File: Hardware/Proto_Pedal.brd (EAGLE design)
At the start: 85.1 x 110.5 mm, 124 parts, among them J1 POWER_JACKSMD_FIXED, Q1 2.5A/30V, SW1 SWITCH-3PDT

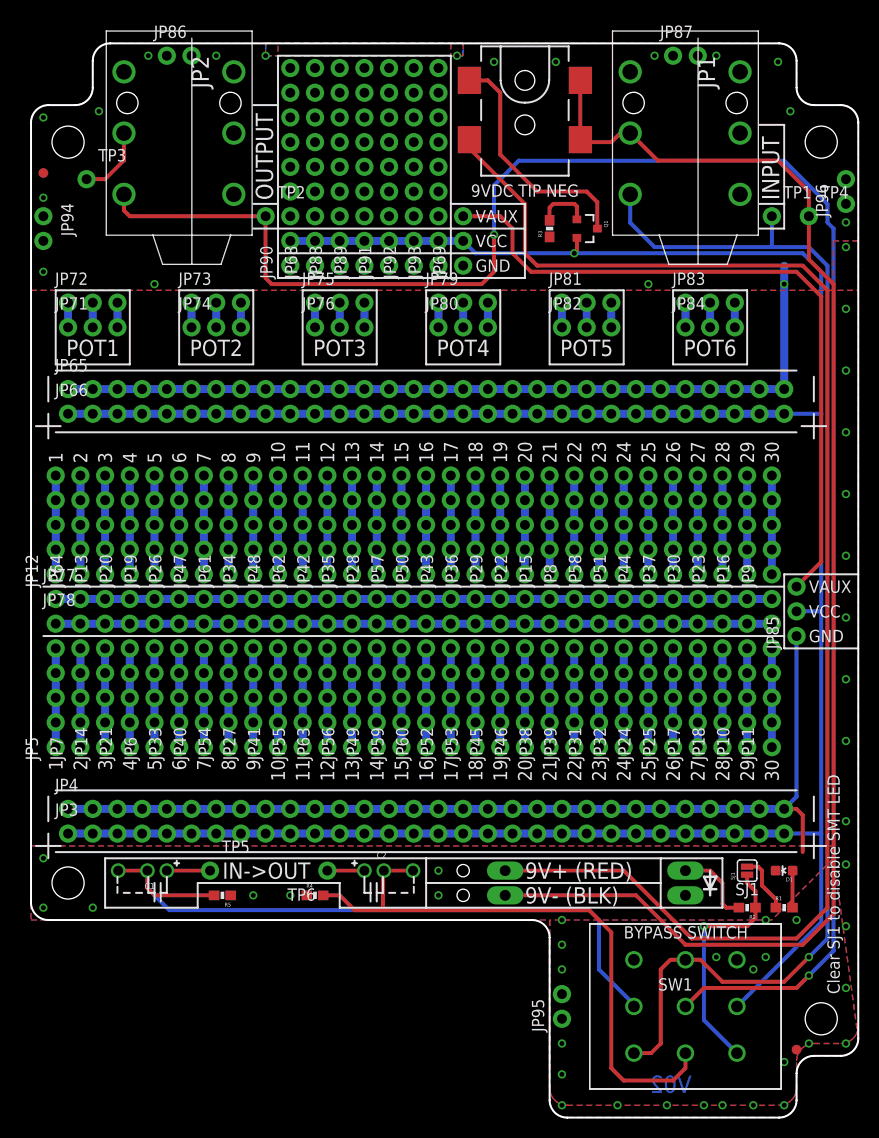
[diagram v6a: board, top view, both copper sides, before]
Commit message: Updates after group review.
PTH power connector.
PTH LED bias resistor.
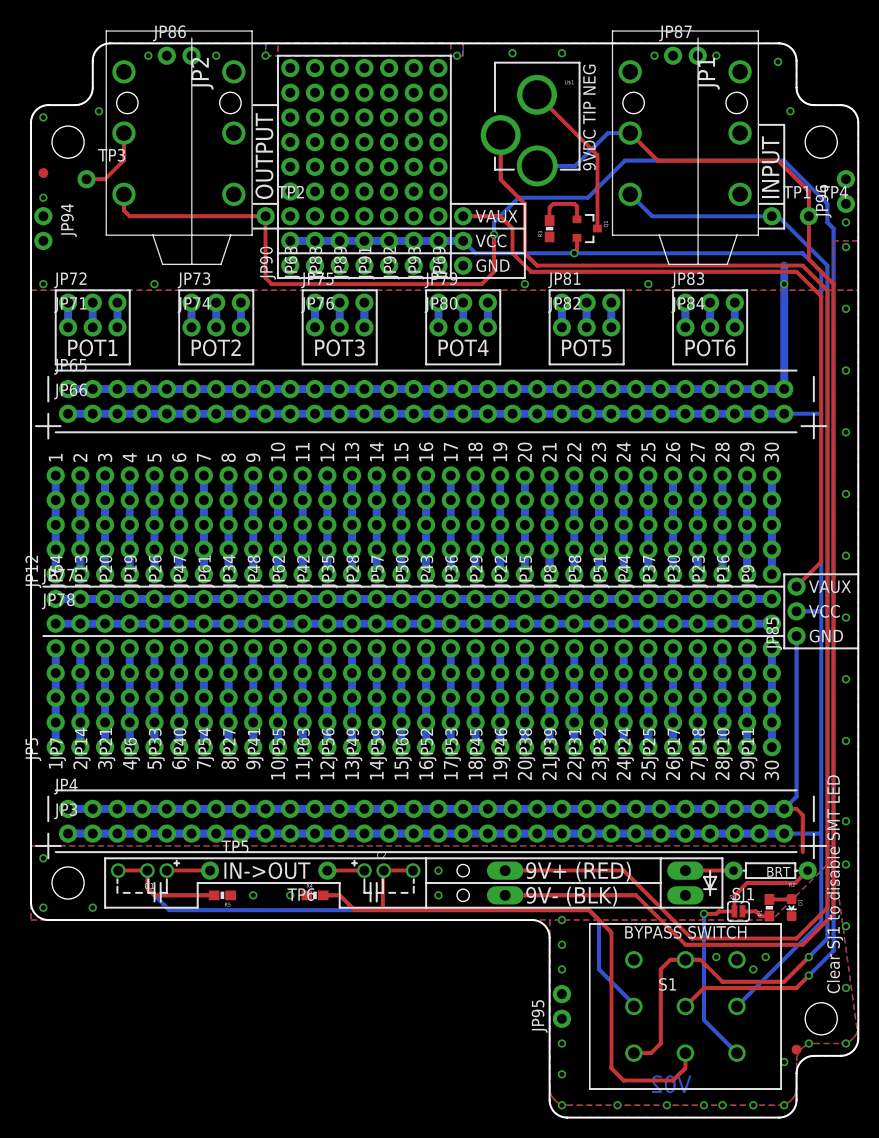
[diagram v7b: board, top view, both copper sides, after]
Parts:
- removed J1: POWER_JACKSMD_FIXED, Testing:POWER_JACK_SMD
- added U$1: POWER_JACK_TIP_NEGATIVE, Testing:POWER-BARRELJACK-PTH-LOCK-FIXED
- R2: value 1K -> BRT; device SparkFun-Resistors:0603-RES -> SparkFun-Resistors:AXIAL-0.3
- moved R2 4.51 mm to (76.1, 25.4)
- moved SJ1 4.28 mm to (72.8, 21.2), turned to 0 degrees
- moved D1 3.89 mm to (78.2, 21.6), turned to 180 degrees
- moved R1 1.52 mm to (75.9, 21.6), turned to 90 degrees
- renumbered SW1 to S1
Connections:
- net LEDA: now also R2.P$2; no longer R2.2
- net N$35: now also R2.P$1; no longer R2.1
- net N$45: now also U$1.SLEEVE-NORMAL; no longer J1.P$4
- net N$55: now also U$1.TIP; no longer J1.VIN0, J1.VIN1
- net VBATT: now also U$1.SLEEVE; no longer J1.GND
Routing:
- net VBATT: track 24.8 -> 16.3 mm
- net N$70: track 128.5 -> 123.7 mm
- net N$35: track 24.9 -> 29.2 mm
- net LEDA: track 8.34 -> 4.95 mm
- net N$65: track 6.10 -> 2.96 mm
- net N$71: track 187.9 -> 185.6 mm
- net N$25: track 3.82 -> 2.30 mm
- net N$45: track 147.6 -> 146.7 mm
- net N$55: track 145.1 -> 144.4 mm
- net GND: vias 58 -> 57

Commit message: Relaxed design to use standard DRU
Fixed funny pour shapes
Relocated a couple traces
Renumbered parts
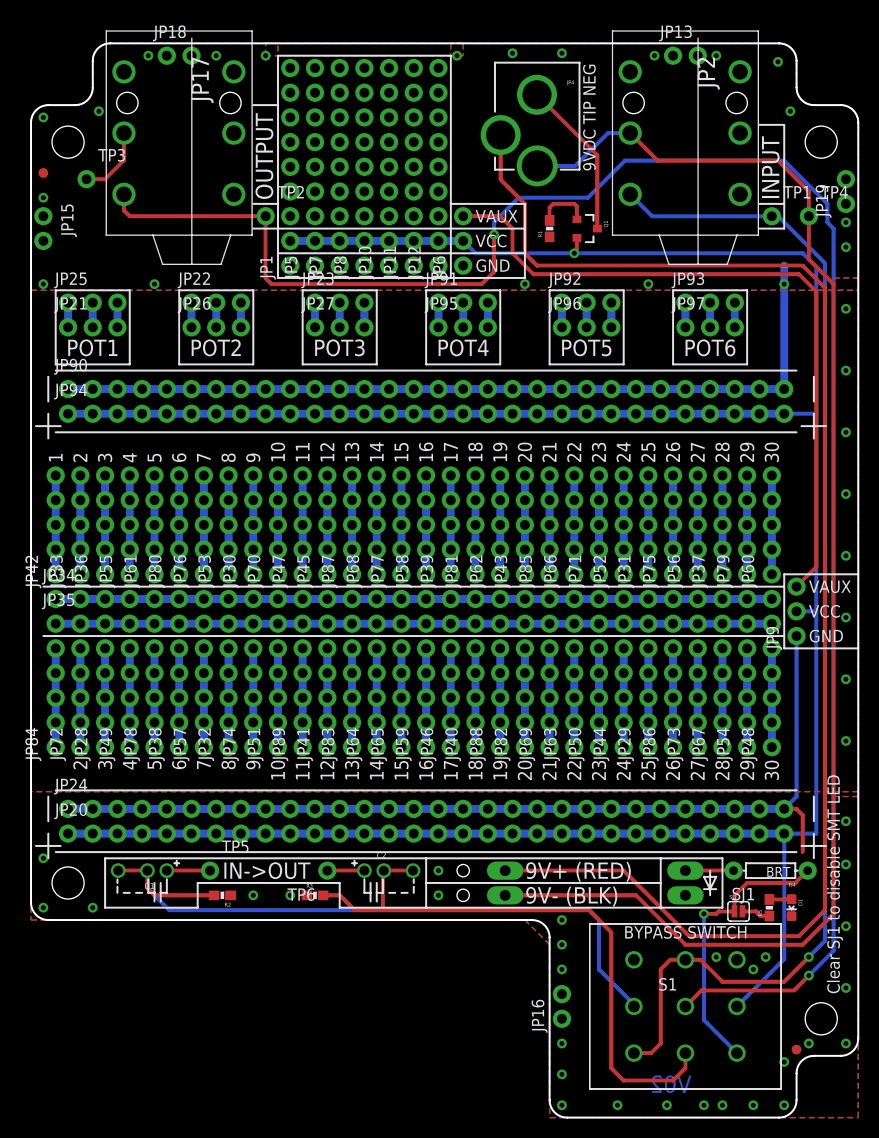
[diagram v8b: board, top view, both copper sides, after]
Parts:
- removed D2: PTH-LED, SparkFun-Connectors:1X02_LONGPADS
- removed U$1: POWER_JACK_TIP_NEGATIVE, Testing:POWER-BARRELJACK-PTH-LOCK-FIXED
- added JP67: 1x5, SparkFun-Connectors:1X05_NO_SILK
- added JP97: 1x3, SparkFun-Connectors:1X03_NO_SILK
- JP1: value INPUT JACK -> 1x9; device SparkFun-Connectors:AUDIO-JACK-.25-INCH-HORIZ-PTH -> SparkFun-Connectors:1X09_NO_SILK
- JP10, JP11, JP12, JP5, JP7, JP8: value 1x5 -> 1x9; device SparkFun-Connectors:1X05_NO_SILK -> SparkFun-Connectors:1X09_NO_SILK
- JP13, JP15, JP16, JP18, JP19: value 1x5 -> 1x2; device SparkFun-Connectors:1X05_NO_SILK -> SparkFun-Connectors:1X02_NO_SILK
- JP14: value 1x5 -> PTH-LED; device SparkFun-Connectors:1X05_NO_SILK -> SparkFun-Connectors:1X02_LONGPADS
- JP17: value 1x5 -> OUTPUT JACK; device SparkFun-Connectors:1X05_NO_SILK -> SparkFun-Connectors:AUDIO-JACK-.25-INCH-HORIZ-PTH
- JP2: value OUTPUT JACK -> INPUT JACK
- JP20, JP24, JP34, JP35: value 1x5 -> 1x30; device SparkFun-Connectors:1X05_NO_SILK -> SparkFun-Connectors:1X30_NO_SILK
- JP21, JP22, JP23, JP25, JP26, JP27, JP6, JP9: value 1x5 -> 1x3; device SparkFun-Connectors:1X05_NO_SILK -> SparkFun-Connectors:1X03_NO_SILK
- JP3: value 1x30 -> 9VBattery; device SparkFun-Connectors:1X30_NO_SILK -> SparkFun-Connectors:1X02_LONGPADS
- JP4: value 1x30 -> POWER_JACK_TIP_NEGATIVE; device SparkFun-Connectors:1X30_NO_SILK -> Testing:POWER-BARRELJACK-PTH-LOCK-FIXED
- JP55: value v -> 1x5
- JP65, JP66, JP77, JP78: value 1x30 -> 1x5; device SparkFun-Connectors:1X30_NO_SILK -> SparkFun-Connectors:1X05_NO_SILK
- JP68, JP88: value 1x9 -> 1x5; device SparkFun-Connectors:1X09_NO_SILK -> SparkFun-Connectors:1X05_NO_SILK
- JP69, JP71, JP72, JP73, JP74, JP75, JP76, JP79, JP80, JP81, JP82, JP83, JP84, JP85: value 1x3 -> 1x5; device SparkFun-Connectors:1X03_NO_SILK -> SparkFun-Connectors:1X05_NO_SILK
- JP70: value 9VBattery -> 1x5; device SparkFun-Connectors:1X02_LONGPADS -> SparkFun-Connectors:1X05_NO_SILK
- JP86, JP87: value 1x2 -> 1x5; device SparkFun-Connectors:1X02_NO_SILK -> SparkFun-Connectors:1X05_NO_SILK
- JP89: value 1x9 -> v; device SparkFun-Connectors:1X09_NO_SILK -> SparkFun-Connectors:1X05_NO_SILK
- JP90: value 1x9 -> 1x30; device SparkFun-Connectors:1X09_NO_SILK -> SparkFun-Connectors:1X30_NO_SILK
- JP91, JP92, JP93: value 1x9 -> 1x3; device SparkFun-Connectors:1X09_NO_SILK -> SparkFun-Connectors:1X03_NO_SILK
- JP94: value 1x2 -> 1x30; device SparkFun-Connectors:1X02_NO_SILK -> SparkFun-Connectors:1X30_NO_SILK
- JP95, JP96: value 1x2 -> 1x3; device SparkFun-Connectors:1X02_NO_SILK -> SparkFun-Connectors:1X03_NO_SILK
- R1: value 1K -> 1M
- R2: value BRT -> 1M; device SparkFun-Resistors:AXIAL-0.3 -> SparkFun-Resistors:0603-RES
- R4: value 1M -> BRT; device SparkFun-Resistors:0603-RES -> SparkFun-Resistors:AXIAL-0.3
- R5: value 1M -> 1K
- moved FID1 118.9 mm to (78.7, 6.99)
- moved FID2 118.9 mm to (1.27, 97.2)
- moved STANDOFF2 108.7 mm to (3.81, 24.1)
- moved JP4 93.4 mm to (52.1, 111.8), turned to 180 degrees
- moved JP18 91.2 mm to (14.0, 109.2), turned to 0 degrees
- moved JP17 90.2 mm to (16.5, 111.8), turned to 270 degrees
- moved JP86 88.1 mm to (66.0, 38.1), turned to 90 degrees
- moved JP19 80.7 mm to (83.8, 94.0)
- moved JP13 79.1 mm to (66.0, 109.2), turned to 0 degrees
- moved JP84 77.8 mm to (2.54, 38.1), turned to 90 degrees
- moved STANDOFF3 77.5 mm to (81.3, 100.3)
- moved JP25 77.2 mm to (3.81, 83.8), turned to 0 degrees
- moved STANDOFF4 76.2 mm to (3.81, 100.3)
- moved R1 73.4 mm to (53.3, 91.4)
- moved R3 72.7 mm to (29.2, 22.9), turned to 0 degrees
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- renumbered LOGO3 to LOGO2
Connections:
- removed net N$10 (its old number): JP9.1, JP9.2, JP9.3, JP9.4, JP9.5
- removed net N$11 (its old number): JP11.1, JP11.2, JP11.3, JP11.4, JP11.5
- removed net N$12 (its old number): JP12.1, JP12.2, JP12.3, JP12.4, JP12.5
- removed net N$13 (its old number): JP13.1, JP13.2, JP13.3, JP13.4, JP13.5
- removed net N$14 (its old number): JP14.1, JP14.2, JP14.3, JP14.4, JP14.5
- removed net N$19 (its old number): JP19.1, JP19.2, JP19.3, JP19.4, JP19.5
- removed net N$20 (its old number): JP20.1, JP20.2, JP20.3, JP20.4, JP20.5
- removed net N$21 (its old number): JP21.1, JP21.2, JP21.3, JP21.4, JP21.5
- removed net N$22 (its old number): JP22.1, JP22.2, JP22.3, JP22.4, JP22.5
- removed net N$23 (its old number): JP23.1, JP23.2, JP23.3, JP23.4, JP23.5
- removed net N$24 (its old number): JP24.1, JP24.2, JP24.3, JP24.4, JP24.5
- removed net N$34 (its old number): JP34.1, JP34.2, JP34.3, JP34.4, JP34.5
- removed net N$5 (its old number): JP10.1, JP10.2, JP10.3, JP10.4, JP10.5
- new net N$15: JP89.1, JP89.2, JP89.3, JP89.4, JP89.5
- new net N$28: JP68.1, JP68.2, JP68.3, JP68.4, JP68.5
- new net N$36: JP81.1, JP81.2, JP81.3, JP81.4, JP81.5
- new net N$37: JP75.1, JP75.2, JP75.3, JP75.4, JP75.5
- new net N$38: JP69.1, JP69.2, JP69.3, JP69.4, JP69.5
- new net N$46: JP82.1, JP82.2, JP82.3, JP82.4, JP82.5
- new net N$47: JP76.1, JP76.2, JP76.3, JP76.4, JP76.5
- new net N$48: JP70.1, JP70.2, JP70.3, JP70.4, JP70.5
- new net N$56: JP83.1, JP83.2, JP83.3, JP83.4, JP83.5
- new net N$57: JP77.1, JP77.2, JP77.3, JP77.4, JP77.5
- new net N$58: JP71.1, JP71.2, JP71.3, JP71.4, JP71.5
- new net N$59: JP65.1, JP65.2, JP65.3, JP65.4, JP65.5
- new net N$6: JP88.1, JP88.2, JP88.3, JP88.4, JP88.5
- net FX_IN: now also R2.2; no longer R5.2
- net FX_OUT: now also R3.2; no longer R4.2
- net GND: now also JP1.1, JP10.1, JP11.1, JP12.1, JP13.1, JP13.2, JP14.2, JP15.1, JP15.2, JP16.1, JP16.2, JP17.SLEEVE, JP18.1, JP18.2, JP19.1, JP19.2, JP2.TIP-NORM, JP24.1, JP24.10, JP24.11, JP24.12, JP24.13, JP24.14, JP24.15, JP24.16, JP24.17, JP24.18, JP24.19, JP24.2, JP24.20, JP24.21, JP24.22, JP24.23, JP24.24, JP24.25, JP24.26, JP24.27, JP24.28, JP24.29, JP24.3, JP24.30, JP24.4, JP24.5, JP24.6, JP24.7, JP24.8, JP24.9, JP5.1, JP6.1, JP7.1, JP8.1, JP9.1, JP90.10, JP90.11, JP90.12, JP90.13, JP90.14, JP90.15, JP90.16, JP90.17, JP90.18, JP90.19, JP90.2, JP90.20, JP90.21, JP90.22, JP90.23, JP90.24, JP90.25, JP90.26, JP90.27, JP90.28, JP90.29, JP90.3, JP90.30, JP90.4, JP90.5, JP90.6, JP90.7, JP90.8, JP90.9, R1.1, R2.1; no longer D2.2, JP1.SLEEVE, JP1.TIP-NORM, JP4.1, JP4.10, JP4.11, JP4.12, JP4.13, JP4.14, JP4.15, JP4.16, JP4.17, JP4.18, JP4.19, JP4.2, JP4.20, JP4.21, JP4.22, JP4.23, JP4.24, JP4.25, JP4.26, JP4.27, JP4.28, JP4.29, JP4.3, JP4.30, JP4.4, JP4.5, JP4.6, JP4.7, JP4.8, JP4.9, JP65.1, JP65.10, JP65.11, JP65.12, JP65.13, JP65.14, JP65.15, JP65.16, JP65.17, JP65.18, JP65.19, JP65.2, JP65.20, JP65.21, JP65.22, JP65.23, JP65.24, JP65.25, JP65.26, JP65.27, JP65.28, JP65.29, JP65.3, JP65.30, JP65.4, JP65.5, JP65.6, JP65.7, JP65.8, JP65.9, JP68.1, JP69.1, JP85.1, JP86.1, JP86.2, JP87.1, JP87.2, JP88.1, JP89.1, JP91.1, JP92.1, JP93.1, JP94.1, JP94.2, JP95.1, JP95.2, JP96.1, JP96.2, R4.1, R5.1
- net LEDA: now also JP14.1, R4.P$2; no longer D2.1, R2.P$2
- net N$1: now also JP84.1, JP84.2, JP84.3, JP84.4, JP84.5; no longer JP5.1, JP5.2, JP5.3, JP5.4, JP5.5
- net N$100: now also JP92.3, JP96.3; no longer JP81.3, JP82.3
- net N$101: now also JP93.1, JP97.1; no longer JP83.1, JP84.1
- net N$102: now also JP93.2, JP97.2; no longer JP83.2, JP84.2
- net N$103: now also JP93.3, JP97.3; no longer JP83.3, JP84.3
- net N$16: now also JP79.1, JP79.2, JP79.3, JP79.4, JP79.5; no longer JP16.1, JP16.2, JP16.3, JP16.4, JP16.5
- net N$17: now also JP73.1, JP73.2, JP73.3, JP73.4, JP73.5; no longer JP17.1, JP17.2, JP17.3, JP17.4, JP17.5
- net N$18: now also JP67.1, JP67.2, JP67.3, JP67.4, JP67.5; no longer JP18.1, JP18.2, JP18.3, JP18.4, JP18.5
- net N$2: now also JP85.1, JP85.2, JP85.3, JP85.4, JP85.5; no longer JP15.1, JP15.2, JP15.3, JP15.4, JP15.5
- net N$25: now also R5.2; no longer R1.2
- net N$26: now also JP80.1, JP80.2, JP80.3, JP80.4, JP80.5; no longer JP26.1, JP26.2, JP26.3, JP26.4, JP26.5
- net N$27: now also JP74.1, JP74.2, JP74.3, JP74.4, JP74.5; no longer JP27.1, JP27.2, JP27.3, JP27.4, JP27.5
- net N$3: now also JP86.1, JP86.2, JP86.3, JP86.4, JP86.5; no longer JP25.1, JP25.2, JP25.3, JP25.4, JP25.5
- net N$35: now also R4.P$1; no longer R2.P$1
- net N$4: now also JP87.1, JP87.2, JP87.3, JP87.4, JP87.5; no longer JP35.1, JP35.2, JP35.3, JP35.4, JP35.5
- net N$45: now also JP3.1, JP4.SLEEVE-NORMAL; no longer JP70.1, U$1.SLEEVE-NORMAL
- net N$55: now also JP2.RING, JP3.2, JP4.TIP; no longer JP1.RING, JP70.2, U$1.TIP
- net N$65: now also R5.1; no longer R1.1
- net N$66: now also JP17.RING; no longer JP2.RING
- net N$7: now also JP78.1, JP78.2, JP78.3, JP78.4, JP78.5; no longer JP6.1, JP6.2, JP6.3, JP6.4, JP6.5
- net N$70: now also JP2.TIP; no longer JP1.TIP
- net N$71: now also JP17.TIP; no longer JP2.TIP
- net N$75: now also R1.2; no longer R3.2
- net N$77: now also JP21.1, JP25.1; no longer JP71.1, JP72.1
- net N$79: now also JP21.2, JP25.2; no longer JP71.2, JP72.2
- net N$8: now also JP72.1, JP72.2, JP72.3, JP72.4, JP72.5; no longer JP7.1, JP7.2, JP7.3, JP7.4, JP7.5
- net N$81: now also JP21.3, JP25.3; no longer JP71.3, JP72.3
- net N$83: now also JP22.1, JP26.1; no longer JP73.1, JP74.1
- net N$85: now also JP22.2, JP26.2; no longer JP73.2, JP74.2
- net N$87: now also JP22.3, JP26.3; no longer JP73.3, JP74.3
- net N$89: now also JP34.1, JP34.10, JP34.11, JP34.12, JP34.13, JP34.14, JP34.15, JP34.16, JP34.17, JP34.18, JP34.19, JP34.2, JP34.20, JP34.21, JP34.22, JP34.23, JP34.24, JP34.25, JP34.26, JP34.27, JP34.28, JP34.29, JP34.3, JP34.30, JP34.4, JP34.5, JP34.6, JP34.7, JP34.8, JP34.9; no longer JP77.1, JP77.10, JP77.11, JP77.12, JP77.13, JP77.14, JP77.15, JP77.16, JP77.17, JP77.18, JP77.19, JP77.2, JP77.20, JP77.21, JP77.22, JP77.23, JP77.24, JP77.25, JP77.26, JP77.27, JP77.28, JP77.29, JP77.3, JP77.30, JP77.4, JP77.5, JP77.6, JP77.7, JP77.8, JP77.9
- net N$9: now also JP66.1, JP66.2, JP66.3, JP66.4, JP66.5; no longer JP8.1, JP8.2, JP8.3, JP8.4, JP8.5
- net N$90: now also JP35.1, JP35.10, JP35.11, JP35.12, JP35.13, JP35.14, JP35.15, JP35.16, JP35.17, JP35.18, JP35.19, JP35.2, JP35.20, JP35.21, JP35.22, JP35.23, JP35.24, JP35.25, JP35.26, JP35.27, JP35.28, JP35.29, JP35.3, JP35.30, JP35.4, JP35.5, JP35.6, JP35.7, JP35.8, JP35.9; no longer JP78.1, JP78.10, JP78.11, JP78.12, JP78.13, JP78.14, JP78.15, JP78.16, JP78.17, JP78.18, JP78.19, JP78.2, JP78.20, JP78.21, JP78.22, JP78.23, JP78.24, JP78.25, JP78.26, JP78.27, JP78.28, JP78.29, JP78.3, JP78.30, JP78.4, JP78.5, JP78.6, JP78.7, JP78.8, JP78.9
- net N$91: now also JP23.1, JP27.1; no longer JP75.1, JP76.1
- net N$93: now also JP23.2, JP27.2; no longer JP75.2, JP76.2
- net N$94: now also JP23.3, JP27.3; no longer JP75.3, JP76.3
- net N$95: now also JP91.1, JP95.1; no longer JP79.1, JP80.1
- net N$96: now also JP91.2, JP95.2; no longer JP79.2, JP80.2
- net N$97: now also JP91.3, JP95.3; no longer JP79.3, JP80.3
- net N$98: now also JP92.1, JP96.1; no longer JP81.1, JP82.1
- net N$99: now also JP92.2, JP96.2; no longer JP81.2, JP82.2
- net VAUX: now also JP6.3, JP9.3; no longer JP69.3, JP85.3
- net VBATT: now also JP4.SLEEVE; no longer U$1.SLEEVE
- net VCC: now also JP1.2, JP10.2, JP11.2, JP12.2, JP20.1, JP20.10, JP20.11, JP20.12, JP20.13, JP20.14, JP20.15, JP20.16, JP20.17, JP20.18, JP20.19, JP20.2, JP20.20, JP20.21, JP20.22, JP20.23, JP20.24, JP20.25, JP20.26, JP20.27, JP20.28, JP20.29, JP20.3, JP20.30, JP20.4, JP20.5, JP20.6, JP20.7, JP20.8, JP20.9, JP5.2, JP6.2, JP7.2, JP8.2, JP9.2, JP94.1, JP94.10, JP94.11, JP94.12, JP94.13, JP94.14, JP94.15, JP94.16, JP94.17, JP94.18, JP94.19, JP94.2, JP94.20, JP94.21, JP94.22, JP94.23, JP94.24, JP94.25, JP94.26, JP94.27, JP94.28, JP94.29, JP94.3, JP94.30, JP94.4, JP94.5, JP94.6, JP94.7, JP94.8, JP94.9; no longer JP3.1, JP3.10, JP3.11, JP3.12, JP3.13, JP3.14, JP3.15, JP3.16, JP3.17, JP3.18, JP3.19, JP3.2, JP3.20, JP3.21, JP3.22, JP3.23, JP3.24, JP3.25, JP3.26, JP3.27, JP3.28, JP3.29, JP3.3, JP3.30, JP3.4, JP3.5, JP3.6, JP3.7, JP3.8, JP3.9, JP66.1, JP66.10, JP66.11, JP66.12, JP66.13, JP66.14, JP66.15, JP66.16, JP66.17, JP66.18, JP66.19, JP66.2, JP66.20, JP66.21, JP66.22, JP66.23, JP66.24, JP66.25, JP66.26, JP66.27, JP66.28, JP66.29, JP66.3, JP66.30, JP66.4, JP66.5, JP66.6, JP66.7, JP66.8, JP66.9, JP68.2, JP69.2, JP85.2, JP88.2, JP89.2, JP90.2, JP91.2, JP92.2, JP93.2
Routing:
- net N$58: track 0.00 -> 10.2 mm
- net N$57: track 0.00 -> 10.2 mm
- net N$48: track 0.00 -> 10.2 mm
- net N$47: track 0.00 -> 10.2 mm
- net N$37: track 0.00 -> 10.2 mm
- net N$36: track 0.00 -> 10.2 mm
- net N$34 (its old number): track 10.2 -> 0.00 mm
- net N$28: track 0.00 -> 10.2 mm
- net N$23 (its old number): track 10.2 -> 0.00 mm
- net N$22 (its old number): track 10.2 -> 0.00 mm
- net N$20 (its old number): track 10.2 -> 0.00 mm
- net N$19 (its old number): track 10.2 -> 0.00 mm
- net N$13 (its old number): track 10.2 -> 0.00 mm
- net N$12 (its old number): track 10.2 -> 0.00 mm
- net N$10 (its old number): track 10.2 -> 0.00 mm
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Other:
- board text added: "All Dimensions in inches PCB fits inside a 1590BB type case."
- board text removed: "All Dimensions in inches"
